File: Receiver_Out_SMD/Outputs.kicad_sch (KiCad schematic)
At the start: 14 parts, among them J1 String1, J2 String2, J3 String3, J4 String4, U1 74HC245

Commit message: fix RJ45 LCSC PN
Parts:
- R10, R7, R8, R9: footprint Resistor_SMD:R_0603_1608Metric_Pad1.05x0.95mm_HandSolder -> Resistor_SMD:R_0603_1608Metric_Pad0.98x0.95mm_HandSolder

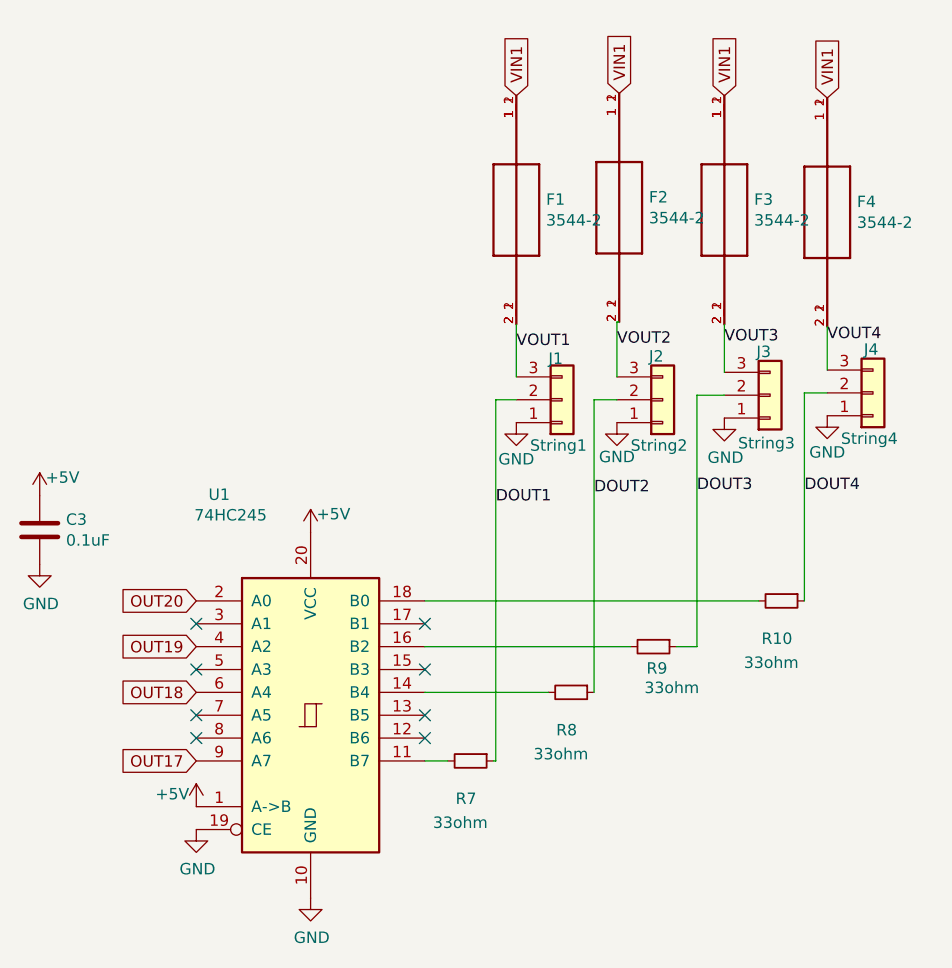
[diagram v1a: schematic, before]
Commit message: switch to 74HCT541
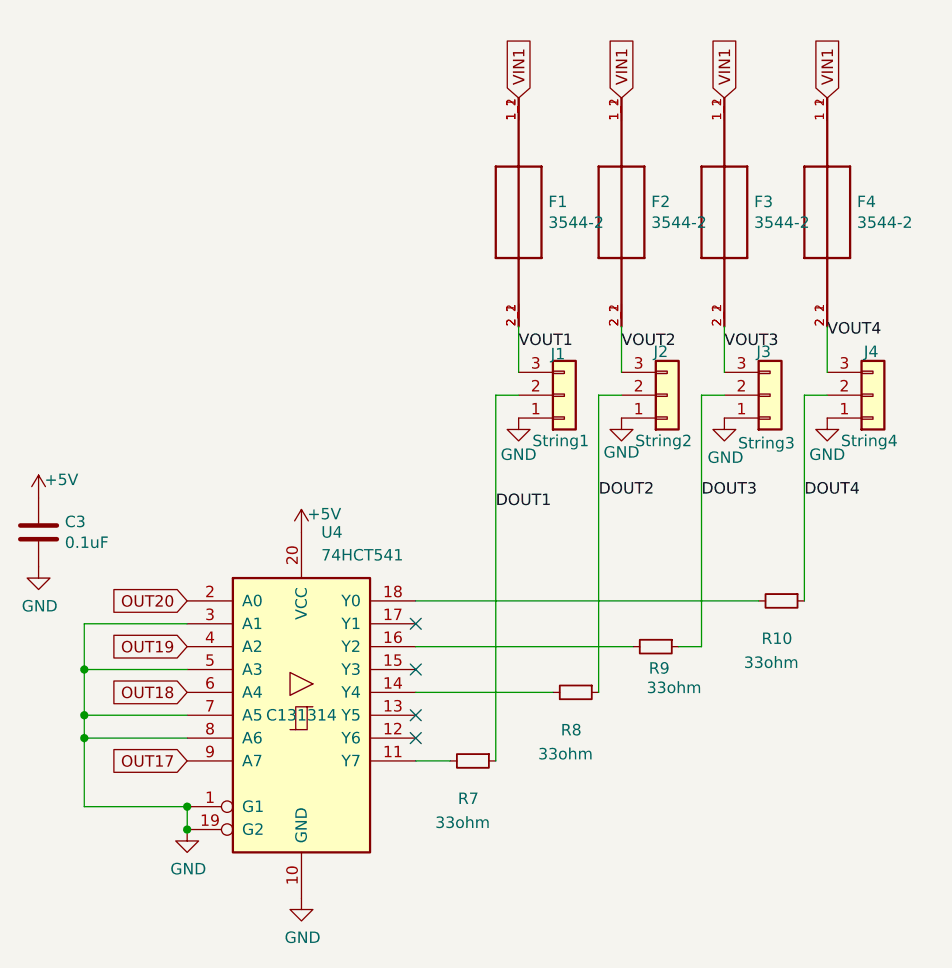
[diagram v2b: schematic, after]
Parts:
- removed U1: 74HC245, Package_SO:SOIC-20W_7.5x12.8mm_P1.27mm, symbol 74xx:74HC245
- added U4: 74HCT541, Package_SO:TSSOP-20_4.4x6.5mm_P0.65mm, symbol 74xx:74HCT541
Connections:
- net +5V: now also U4.20 (VCC)
- net GND: now also U4.1 (G1), U4.10 (GND), U4.19 (G2), U4.3 (A1), U4.5 (A3), U4.7 (A5), U4.8 (A6)
- net OUT17: now also U4.9 (A7)
- net OUT18: now also U4.6 (A4)
- net OUT19: now also U4.4 (A2)
- net OUT20: now also U4.2 (A0)
- net at R7.2: now also U4.11 (Y7)
- net at R8.2: now also U4.14 (Y4)
- net at R10.2: now also U4.18 (Y0)
- net at R9.2: now also U4.16 (Y2)
- no-connect marks 8 -> 4
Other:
- moved on the sheet: F2, J1, J2, R8

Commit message: v3 - Add an Attiny1616 Micro controller and Test Button to enable local testing.
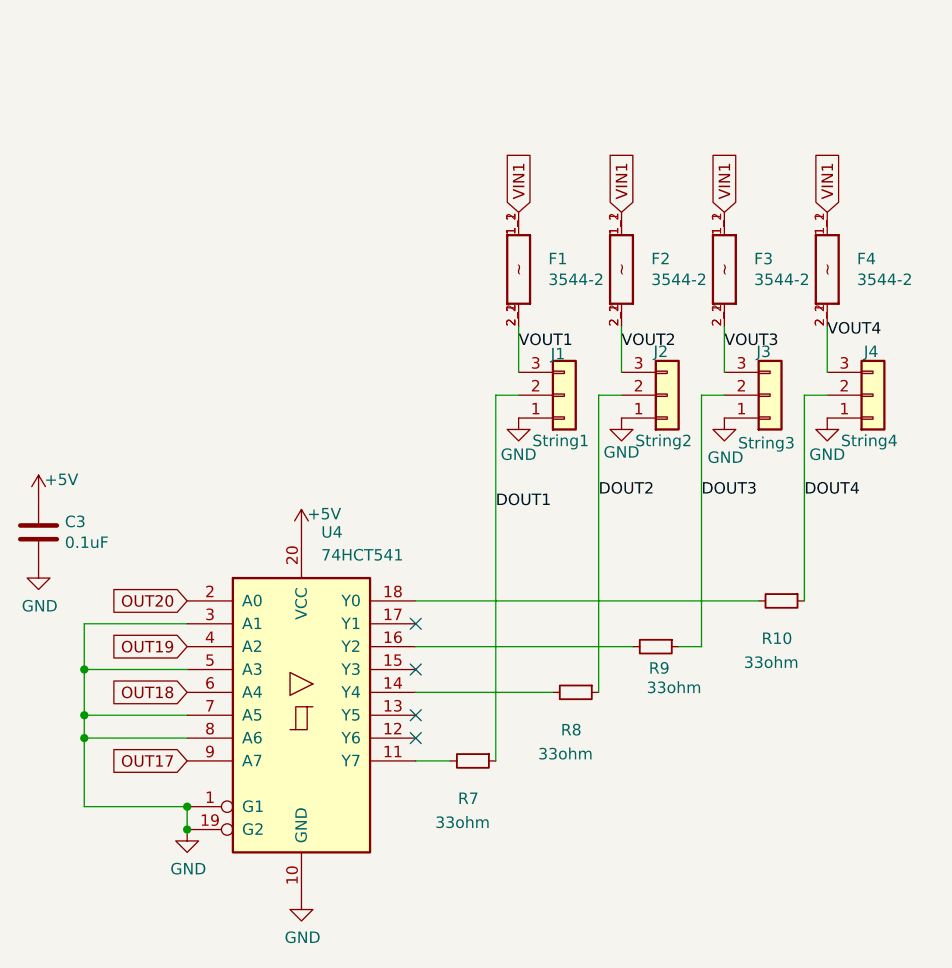
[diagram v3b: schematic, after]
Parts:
- F1, F2, F3, F4: footprint Keystone_Fuse:FUSE_3544-2 -> Scotts:FUSE_3544-2; symbol Receiver_Out-rescue:3544-2-Keystone_Fuse -> Scotts:3544-2; LCSC (none) -> C492610
- R10, R7, R8, R9: footprint Resistor_SMD:R_0603_1608Metric_Pad0.98x0.95mm_HandSolder -> Resistor_SMD:R_0603_1608Metric
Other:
- moved on the sheet: F1, F2, F3, F4

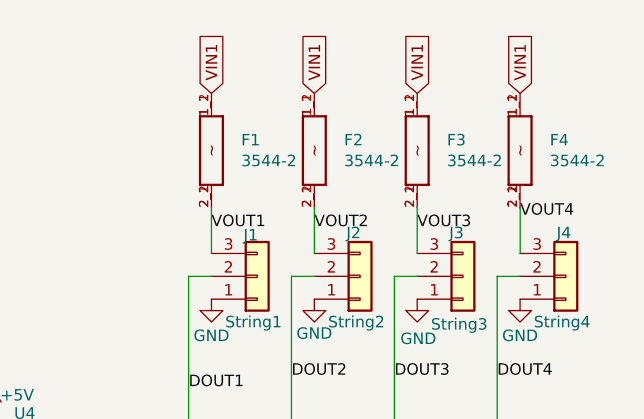
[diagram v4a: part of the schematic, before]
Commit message: move to push connectors and poly fuses
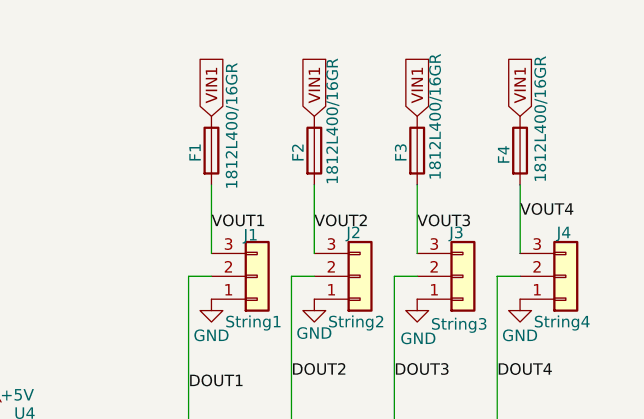
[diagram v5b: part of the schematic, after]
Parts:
- F1, F2, F3, F4: value 3544-2 -> 1812L400/16GR; footprint Scotts:FUSE_3544-2 -> Scotts:Fuse_1812_4532Metric; symbol Scotts:3544-2 -> Device:Fuse; LCSC C492610 -> C22374900; LCSC_PN C492610 -> C22374900
- J1, J2, J3, J4: footprint Connector_Phoenix_MC:PhoenixContact_MCV_1,5_3-G-3.5_1x03_P3.50mm_Vertical -> Scotts:DG250-3.5-03P
- U4: LCSC C131314 -> C436096; LCSC_PN C131314 -> C436096
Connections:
- net VIN1: now also F1.1, F2.1, F3.1, F4.1; no longer F1.1_1 (1), F1.1_2 (1), F2.1_1 (1), F2.1_2 (1), F3.1_1 (1), F3.1_2 (1), F4.1_1 (1), F4.1_2 (1)
- net VOUT1: now also F1.2; no longer F1.2_1 (2), F1.2_2 (2)
- net VOUT2: now also F2.2; no longer F2.2_1 (2), F2.2_2 (2)
- net VOUT3: now also F3.2; no longer F3.2_1 (2), F3.2_2 (2)
- net VOUT4: now also F4.2; no longer F4.2_1 (2), F4.2_2 (2)
